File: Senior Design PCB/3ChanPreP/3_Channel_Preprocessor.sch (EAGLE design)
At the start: 85 parts, among them U1 AD8613AUJZ-R2, U2 AD8619ARZ, U3 AD8613AUJZ-R2, U4 AD8619ARZ, U5 AD8613AUJZ-R2, U6 AD8619ARZ

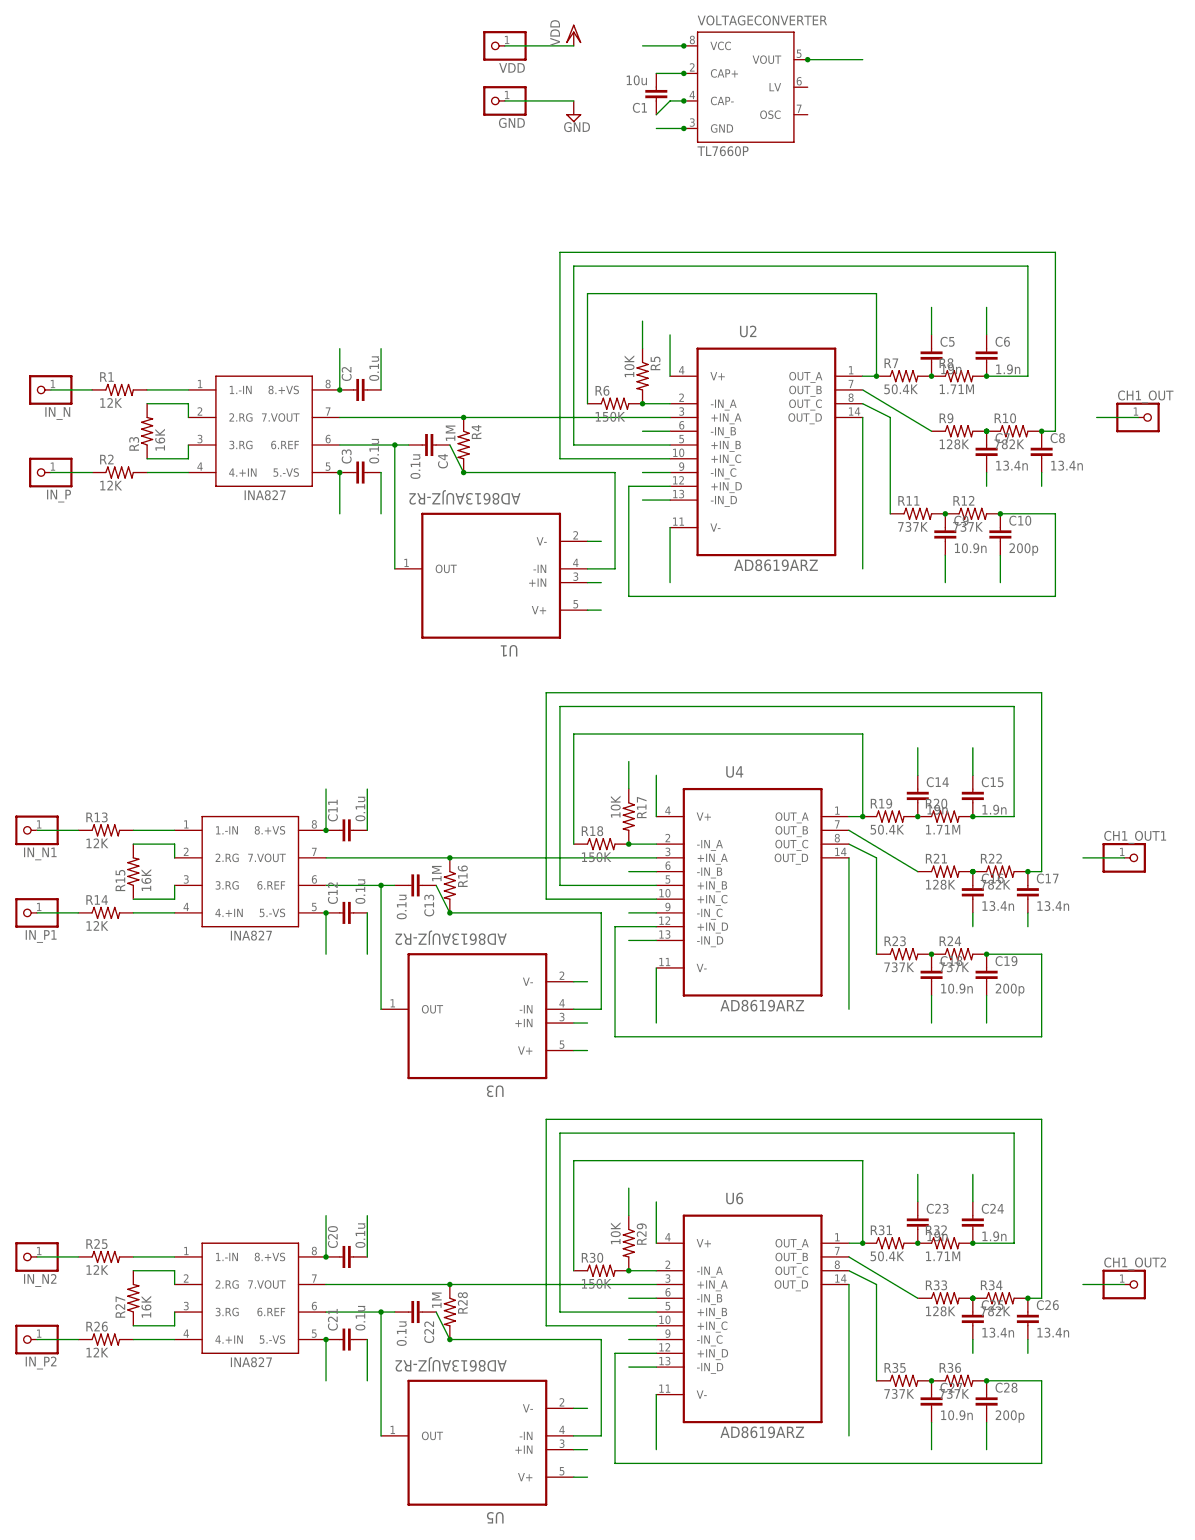
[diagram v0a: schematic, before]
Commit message: Added BOMs, versions for assembly instructions
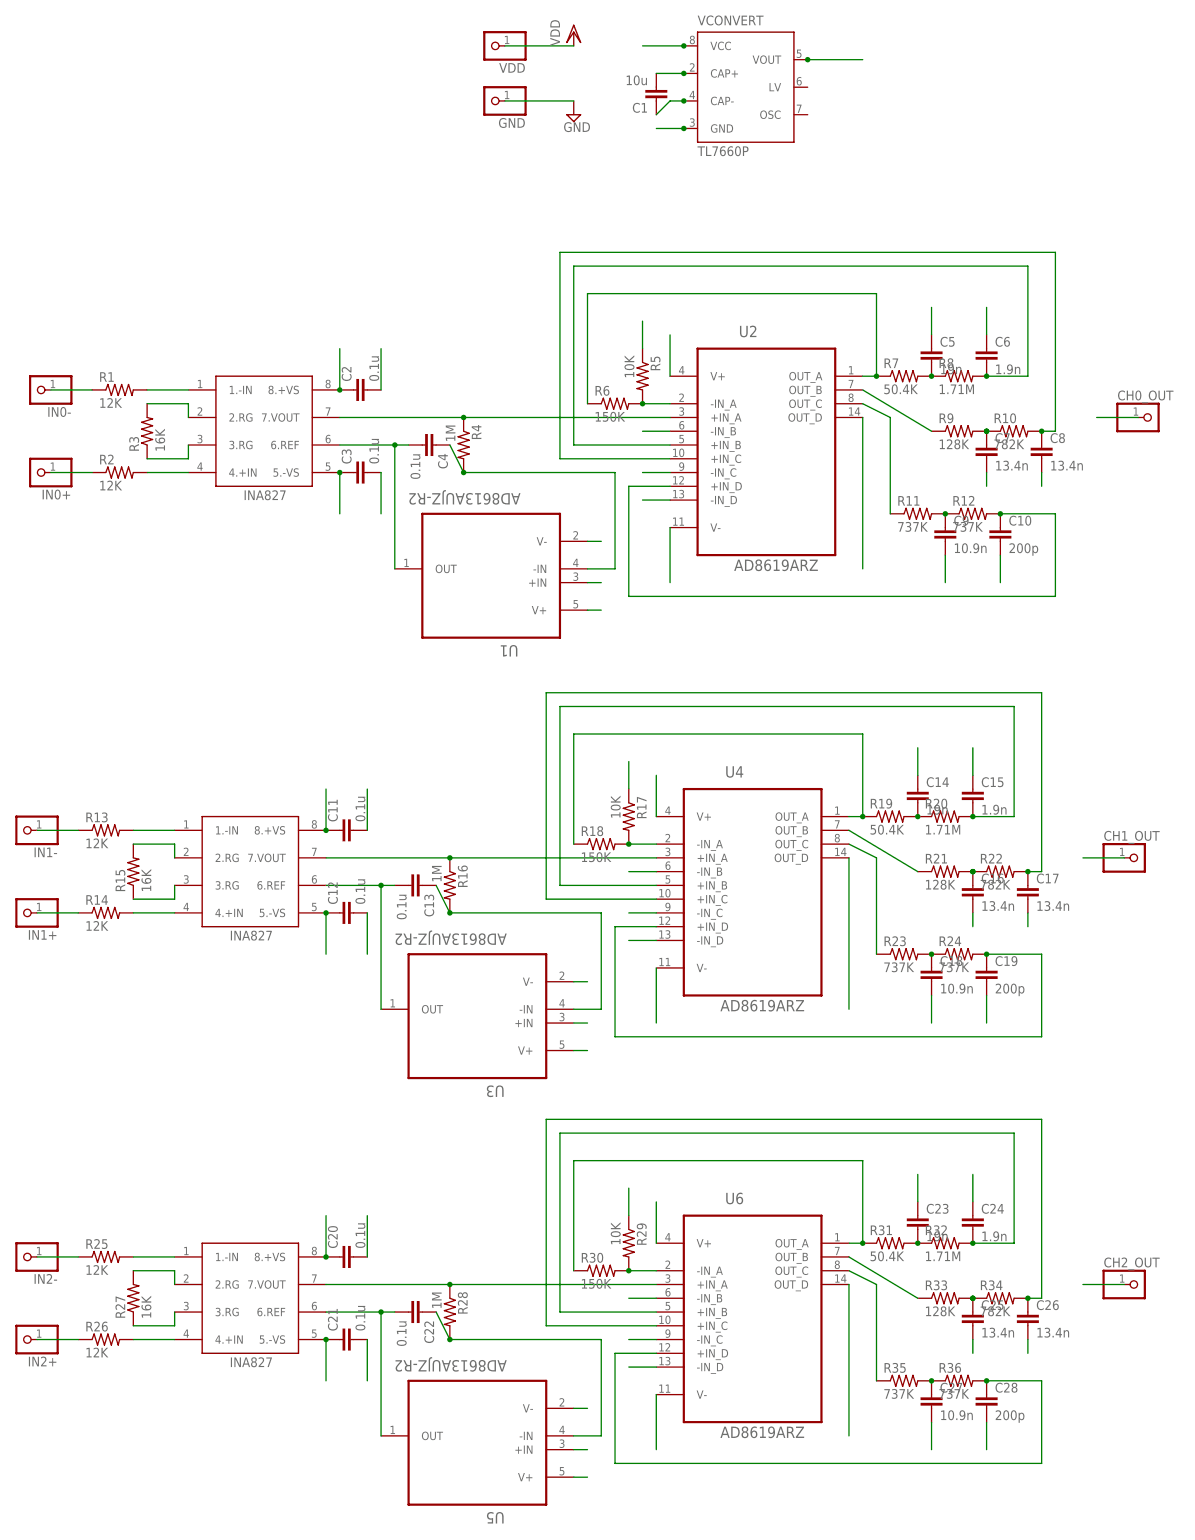
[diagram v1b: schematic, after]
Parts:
- removed CH1_OUT1: (no value), pinhead:PINHD-1X1
- added CH0_OUT: (no value), pinhead:PINHD-1X1
- renumbered CH1_OUT2 to CH2_OUT, IN_N to IN0-, IN_N1 to IN1-, IN_N2 to IN2-, IN_P to IN0+, IN_P1 to IN1+, IN_P2 to IN2+, VOLTAGECONVERTER to VCONVERT
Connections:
- net OUT_D: now also CH0_OUT.1; no longer CH1_OUT.1
- net OUT_D1: now also CH1_OUT.1; no longer CH1_OUT1.1
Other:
- moved on the sheet: CH1_OUT
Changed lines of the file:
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@@
 <?xml version="1.0" encoding="utf-8"?>
 <!DOCTYPE eagle SYSTEM "eagle.dtd">
-<eagle version="8.0.0">
+<eagle version="6.5.0">
 <drawing>
 <settings>
@@
 </classes>
 <parts>
-<part name="VOLTAGECONVERTER" library="texas" deviceset="TL7660" device="P"/>
+<part name="VCONVERT" library="texas" deviceset="TL7660" device="P"/>
 <part name="GND" library="pinhead" deviceset="PINHD-1X1" device=""/>
 <part name="VDD" library="pinhead" deviceset="PINHD-1X1" device=""/>
-<part name="CH1_OUT" library="pinhead" deviceset="PINHD-1X1" device=""/>
-<part name="IN_N" library="pinhead" deviceset="PINHD-1X1" device=""/>
-<part name="IN_P" library="pinhead" deviceset="PINHD-1X1" device=""/>
+<part name="CH0_OUT" library="pinhead" deviceset="PINHD-1X1" device=""/>
+<part name="IN0-" library="pinhead" deviceset="PINHD-1X1" device=""/>
+<part name="IN0+" library="pinhead" deviceset="PINHD-1X1" device=""/>
 <part name="INA1" library="INA827" deviceset="INA827" device=""/>
 <part name="R1" library="rcl" deviceset="R-US_" device="M1206" value="12K"/>
@@
 <part name="SUPPLY1" library="supply2" deviceset="GND" device=""/>
 <part name="VDD1" library="supply1" deviceset="VDD" device=""/>
-<part name="CH1_OUT1" library="pinhead" deviceset="PINHD-1X1" device=""/>
-<part name="IN_N1" library="pinhead" deviceset="PINHD-1X1" device=""/>
-<part name="IN_P1" library="pinhead" deviceset="PINHD-1X1" device=""/>
+<part name="CH1_OUT" library="pinhead" deviceset="PINHD-1X1" device=""/>
+<part name="IN1-" library="pinhead" deviceset="PINHD-1X1" device=""/>
+<part name="IN1+" library="pinhead" deviceset="PINHD-1X1" device=""/>
 <part name="U$2" library="INA827" deviceset="INA827" device=""/>
 <part name="R13" library="rcl" deviceset="R-US_" device="M1206" value="12K"/>
@@
 <part name="C18" library="rcl" deviceset="C-EU" device="C1206" value="10.9n"/>
 <part name="C19" library="rcl" deviceset="C-EU" device="C1206" value="200p"/>
-<part name="CH1_OUT2" library="pinhead" deviceset="PINHD-1X1" device=""/>
-<part name="IN_N2" library="pinhead" deviceset="PINHD-1X1" device=""/>
-<part name="IN_P2" library="pinhead" deviceset="PINHD-1X1" device=""/>
+<part name="CH2_OUT" library="pinhead" deviceset="PINHD-1X1" device=""/>
+<part name="IN2-" library="pinhead" deviceset="PINHD-1X1" device=""/>
+<part name="IN2+" library="pinhead" deviceset="PINHD-1X1" device=""/>
 <part name="U$3" library="INA827" deviceset="INA827" device=""/>
 <part name="R25" library="rcl" deviceset="R-US_" device="M1206" value="12K"/>
@@
 </plain>
 <instances>
-<instance part="VOLTAGECONVERTER" gate="G$1" x="-20.32" y="-91.44"/>
+<instance part="VCONVERT" gate="G$1" x="-20.32" y="-91.44"/>
 <instance part="GND" gate="G$1" x="-66.04" y="-93.98" rot="R180"/>
 <instance part="VDD" gate="G$1" x="-66.04" y="-83.82" rot="R180"/>
-<instance part="CH1_OUT" gate="G$1" x="55.88" y="-152.4"/>
-<instance part="IN_N" gate="G$1" x="-149.86" y="-147.32" rot="R180"/>
-<instance part="IN_P" gate="G$1" x="-149.86" y="-162.56" rot="R180"/>
+<instance part="CH0_OUT" gate="G$1" x="55.88" y="-152.4"/>
+<instance part="IN0-" gate="G$1" x="-149.86" y="-147.32" rot="R180"/>
+<instance part="IN0+" gate="G$1" x="-149.86" y="-162.56" rot="R180"/>
 <instance part="INA1" gate="G$1" x="-96.52" y="-165.1"/>
 <instance part="R1" gate="G$1" x="-134.62" y="-147.32"/>
@@
 <instance part="SUPPLY1" gate="GND" x="-50.8" y="-96.52"/>
 <instance part="VDD1" gate="G$1" x="-50.8" y="-81.28"/>
-<instance part="CH1_OUT1" gate="G$1" x="53.34" y="-233.68"/>
-<instance part="IN_N1" gate="G$1" x="-152.4" y="-228.6" rot="R180"/>
-<instance part="IN_P1" gate="G$1" x="-152.4" y="-243.84" rot="R180"/>
+<instance part="CH1_OUT" gate="G$1" x="53.34" y="-233.68"/>
+<instance part="IN1-" gate="G$1" x="-152.4" y="-228.6" rot="R180"/>
+<instance part="IN1+" gate="G$1" x="-152.4" y="-243.84" rot="R180"/>
 <instance part="U$2" gate="G$1" x="-99.06" y="-246.38"/>
 <instance part="R13" gate="G$1" x="-137.16" y="-228.6"/>
@@
 <instance part="C18" gate="G$1" x="15.24" y="-254"/>
 <instance part="C19" gate="G$1" x="25.4" y="-254"/>
-<instance part="CH1_OUT2" gate="G$1" x="53.34" y="-312.42"/>
-<instance part="IN_N2" gate="G$1" x="-152.4" y="-307.34" rot="R180"/>
-<instance part="IN_P2" gate="G$1" x="-152.4" y="-322.58" rot="R180"/>
+<instance part="CH2_OUT" gate="G$1" x="53.34" y="-312.42"/>
+<instance part="IN2-" gate="G$1" x="-152.4" y="-307.34" rot="R180"/>
+<instance part="IN2+" gate="G$1" x="-152.4" y="-322.58" rot="R180"/>
 <instance part="U$3" gate="G$1" x="-99.06" y="-325.12"/>
 <instance part="R25" gate="G$1" x="-137.16" y="-307.34"/>
@@
 <net name="GND" class="0">
 <segment>
-<pinref part="VOLTAGECONVERTER" gate="G$1" pin="GND"/>
+<pinref part="VCONVERT" gate="G$1" pin="GND"/>
 <wire x1="-35.56" y1="-99.06" x2="-30.48" y2="-99.06" width="0.1524" layer="91"/>
 <junction x="-30.48" y="-99.06"/>
@@
 <net name="VDD" class="0">
 <segment>
-<pinref part="VOLTAGECONVERTER" gate="G$1" pin="VCC"/>
+<pinref part="VCONVERT" gate="G$1" pin="VCC"/>
 <wire x1="-30.48" y1="-83.82" x2="-38.1" y2="-83.82" width="0.1524" layer="91"/>
 <junction x="-30.48" y="-83.82"/>
@@
 <net name="N$1" class="0">
 <segment>
-<pinref part="VOLTAGECONVERTER" gate="G$1" pin="CAP+"/>
+<pinref part="VCONVERT" gate="G$1" pin="CAP+"/>
 <wire x1="-30.48" y1="-88.9" x2="-35.56" y2="-88.9" width="0.1524" layer="91"/>
 <junction x="-30.48" y="-88.9"/>
@@
 <net name="N$2" class="0">
 <segment>
-<pinref part="VOLTAGECONVERTER" gate="G$1" pin="CAP-"/>
+<pinref part="VCONVERT" gate="G$1" pin="CAP-"/>
 <wire x1="-30.48" y1="-93.98" x2="-33.02" y2="-93.98" width="0.1524" layer="91"/>
 <wire x1="-33.02" y1="-93.98" x2="-35.56" y2="-96.52" width="0.1524" layer="91"/>
@@
 <net name="VDD-" class="0">
 <segment>
-<pinref part="VOLTAGECONVERTER" gate="G$1" pin="VOUT"/>
+<pinref part="VCONVERT" gate="G$1" pin="VOUT"/>
 <wire x1="-7.62" y1="-86.36" x2="2.54" y2="-86.36" width="0.1524" layer="91"/>
 <junction x="-7.62" y="-86.36"/>
@@
 <net name="IN_P" class="0">
 <segment>
-<pinref part="IN_P" gate="G$1" pin="1"/>
+<pinref part="IN0+" gate="G$1" pin="1"/>
 <wire x1="-147.32" y1="-162.56" x2="-139.7" y2="-162.56" width="0.1524" layer="91"/>
 <pinref part="R2" gate="G$1" pin="1"/>
@@
 <net name="IN_N" class="0">
 <segment>
-<pinref part="IN_N" gate="G$1" pin="1"/>
+<pinref part="IN0-" gate="G$1" pin="1"/>
 <pinref part="R1" gate="G$1" pin="1"/>
 <wire x1="-139.7" y1="-147.32" x2="-147.32" y2="-147.32" width="0.1524" layer="91"/>
@@
 </segment>
 <segment>
-<pinref part="CH1_OUT" gate="G$1" pin="1"/>
+<pinref part="CH0_OUT" gate="G$1" pin="1"/>
 <wire x1="53.34" y1="-152.4" x2="45.72" y2="-152.4" width="0.1524" layer="91"/>
 </segment>
@@
 <net name="IN_P1" class="0">
 <segment>
-<pinref part="IN_P1" gate="G$1" pin="1"/>
+<pinref part="IN1+" gate="G$1" pin="1"/>
 <wire x1="-149.86" y1="-243.84" x2="-142.24" y2="-243.84" width="0.1524" layer="91"/>
 <pinref part="R14" gate="G$1" pin="1"/>
@@
 <net name="IN_N1" class="0">
 <segment>
-<pinref part="IN_N1" gate="G$1" pin="1"/>
+<pinref part="IN1-" gate="G$1" pin="1"/>
 <pinref part="R13" gate="G$1" pin="1"/>
 <wire x1="-142.24" y1="-228.6" x2="-149.86" y2="-228.6" width="0.1524" layer="91"/>
@@
 </segment>
 <segment>
-<pinref part="CH1_OUT1" gate="G$1" pin="1"/>
+<pinref part="CH1_OUT" gate="G$1" pin="1"/>
 <wire x1="50.8" y1="-233.68" x2="43.18" y2="-233.68" width="0.1524" layer="91"/>
 </segment>
@@
 <net name="IN_P2" class="0">
 <segment>
-<pinref part="IN_P2" gate="G$1" pin="1"/>
+<pinref part="IN2+" gate="G$1" pin="1"/>
 <wire x1="-149.86" y1="-322.58" x2="-142.24" y2="-322.58" width="0.1524" layer="91"/>
 <pinref part="R26" gate="G$1" pin="1"/>
@@
 <net name="IN_N2" class="0">
 <segment>
-<pinref part="IN_N2" gate="G$1" pin="1"/>
+<pinref part="IN2-" gate="G$1" pin="1"/>
 <pinref part="R25" gate="G$1" pin="1"/>
 <wire x1="-142.24" y1="-307.34" x2="-149.86" y2="-307.34" width="0.1524" layer="91"/>
@@
 </segment>
 <segment>
-<pinref part="CH1_OUT2" gate="G$1" pin="1"/>
+<pinref part="CH2_OUT" gate="G$1" pin="1"/>
 <wire x1="50.8" y1="-312.42" x2="43.18" y2="-312.42" width="0.1524" layer="91"/>
 </segment>
